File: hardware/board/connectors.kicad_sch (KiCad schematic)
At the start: 15 parts, among them J6 USB C/USB 2.0, J7 Big button

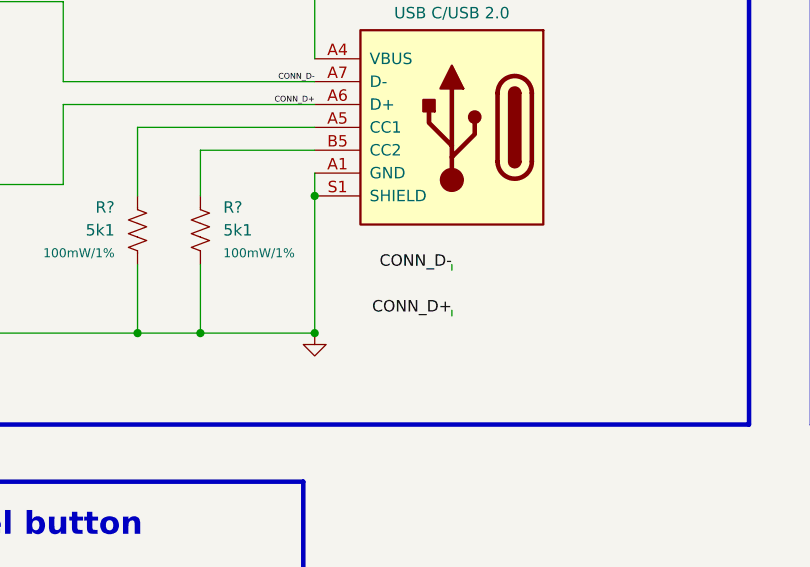
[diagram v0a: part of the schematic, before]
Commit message: hardware: change USB connector, change flash chip, change SPI flash pin assignments, other small updates to routing
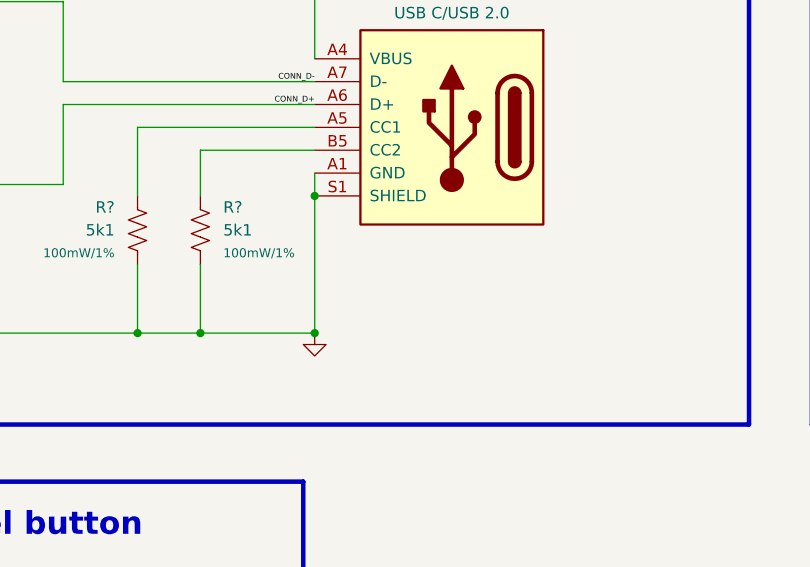
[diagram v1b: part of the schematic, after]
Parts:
- J6: footprint Connector_USB:USB_C_Receptacle_GCT_USB4115-03-C -> winterbloom:USB_C_Vertical_GT-USB-7038X; MPN https://www.digikey.com/en/products/detail/gct/USB4115-03-C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 -> GT-USB-7038D, MC-110LD-L124, GT-USB-7038E, GT-USB-7038F, MC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
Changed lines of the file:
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@@
-    (stroke (width 0) (type default))
-  )
-  (wire (pts (xy 125.73 61.595) (xy 125.73 60.96))
     (stroke (width 0) (type default))
   )
@@
   )
   (wire (pts (xy 187.325 44.45) (xy 195.58 44.45))
-    (stroke (width 0) (type default))
-  )
-  (wire (pts (xy 125.73 66.675) (xy 125.73 66.04))
     (stroke (width 0) (type default))
   )
@@
     (effects (font (size 0.64 0.64)) (justify right bottom))
   )
-  (label "CONN_D-" (at 125.73 61.595 180) (fields_autoplaced)
-    (effects (font (size 1.27 1.27)) (justify right bottom))
-  )
   (label "BUTTON_DOTSTAR_DATA" (at 40.64 104.14 180) (fields_autoplaced)
     (effects (font (size 1.27 1.27)) (justify right bottom))
@@
   )
   (label "BUTTON_DOTSTAR_CLK" (at 40.64 106.68 180) (fields_autoplaced)
-    (effects (font (size 1.27 1.27)) (justify right bottom))
-  )
-  (label "CONN_D+" (at 125.73 66.675 180) (fields_autoplaced)
     (effects (font (size 1.27 1.27)) (justify right bottom))
   )
@@
       (effects (font (size 1.27 1.27)))
     )
-    (property "Footprint" "Connector_USB:USB_C_Receptacle_GCT_USB4115-03-C" (at 121.92 46.99 0)
-      (effects (font (size 1.27 1.27)) hide)
-    )
-    (property "Datasheet" "https://www.usb.org/sites/default/files/documents/usb_type-c.zip" (at 121.92 45.72 0)
-      (effects (font (size 1.27 1.27)) hide)
-    )
-    (property "MPN" "https://www.digikey.com/en/products/detail/gct/USB4115-03-C/13557449" (at 125.73 45.72 0)
-      (effects (font (size 1.27 1.27)) hide)
-    )
+    (property "Footprint" "winterbloom:USB_C_Vertical_GT-USB-7038X" (at 121.92 46.99 0)
+      (effects (font (size 1.27 1.27)) hide)
+    )
+    (property "Datasheet" "https://datasheet.lcsc.com/lcsc/2203281830_G-Switch-GT-USB-7038F_C2982478.pdf" (at 121.92 45.72 0)
+      (effects (font (size 1.27 1.27)) hide)
+    )
+    (property "MPN" "GT-USB-7038D, MC-110LD-L124, GT-USB-7038E, GT-USB-7038F, MC-110LD-L131, MC-110LD-L137" (at 125.73 45.72 0)
+      (effects (font (size 1.27 1.27)) hide)
+    )

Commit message: hardware: rename to Goosehonk Nebula, prep v7
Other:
- company: (none) -> Winterbloom
- title: (none) -> Goosehonk Nebula
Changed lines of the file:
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@@
 (kicad_sch (version 20230121) (generator eeschema)
-  (paper "A4")
+  (paper "USLetter")
+  (title_block
+    (title "Goosehonk Nebula")
+    (date "2023-10-08")
+    (rev "v7")
+    (company "Winterbloom")
+    (comment 1 "Alethea Flowers")
+    (comment 2 "CERN-OHL-P V2")
+    (comment 3 "goose.wntr.dev")
+  )
   (junction (at 70.485 52.07) (diameter 0) (color 0 0 0 0)
   )
